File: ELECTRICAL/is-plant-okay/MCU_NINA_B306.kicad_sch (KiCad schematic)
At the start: 1 part

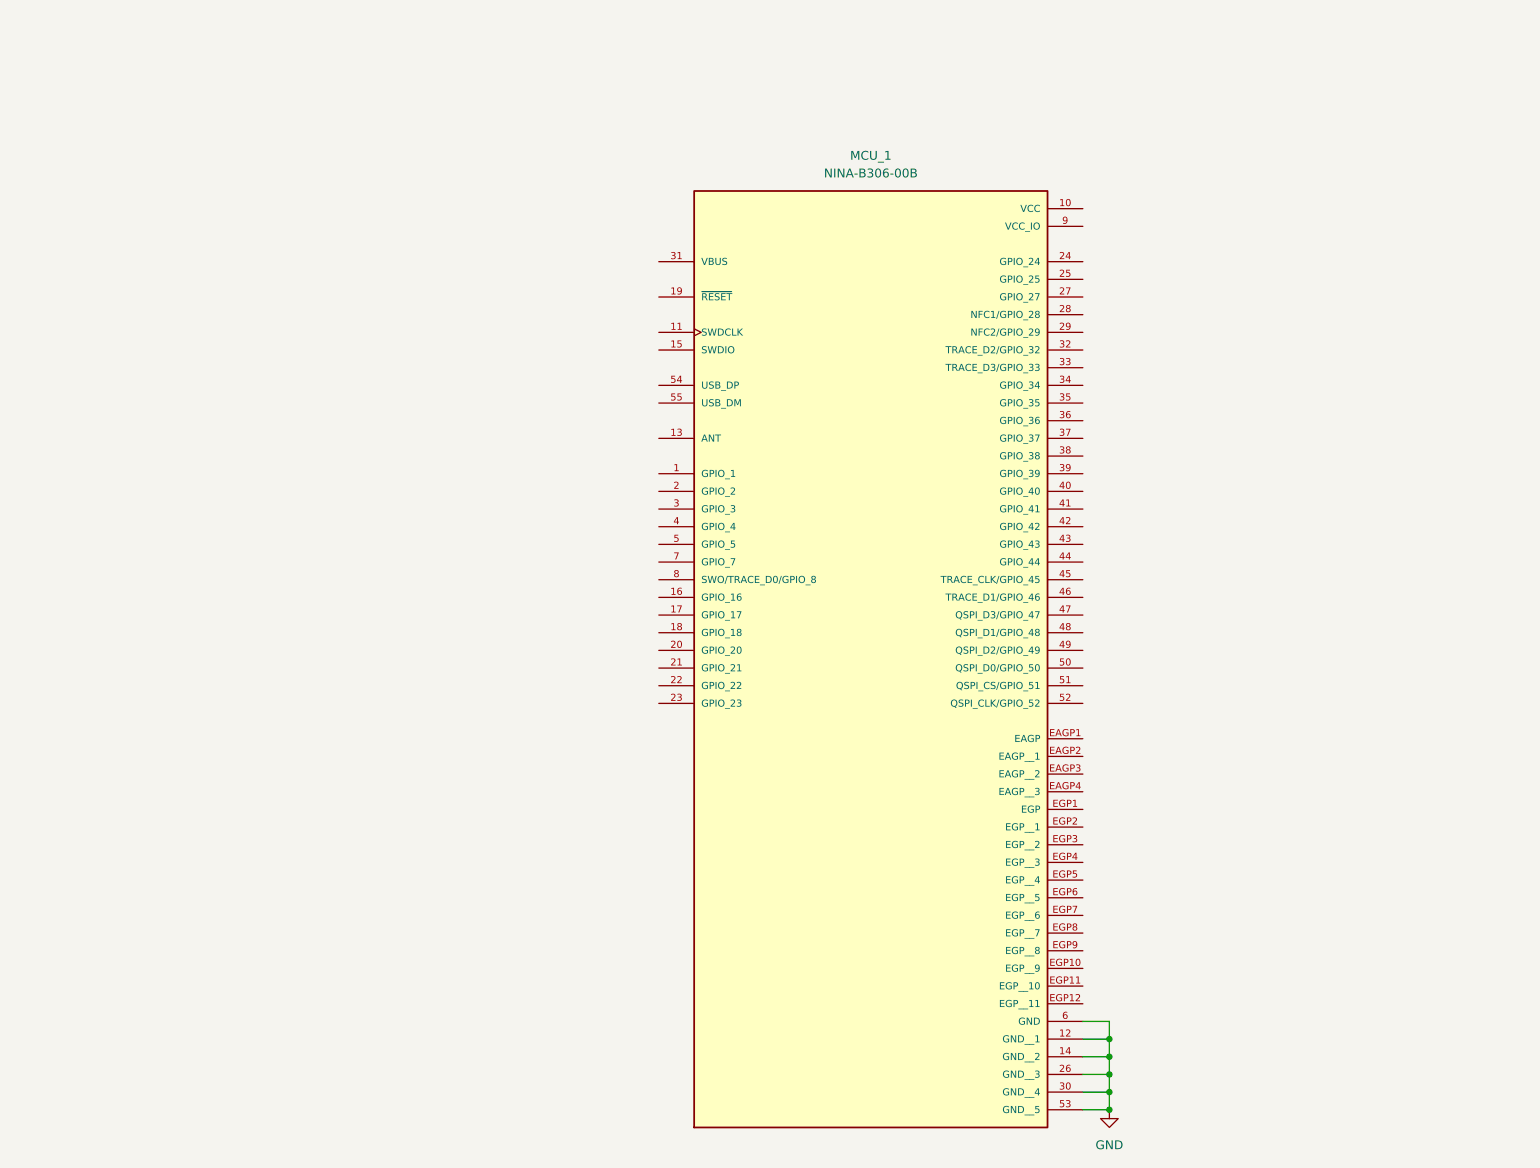
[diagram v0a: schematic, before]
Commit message: feat: add pins for mcu
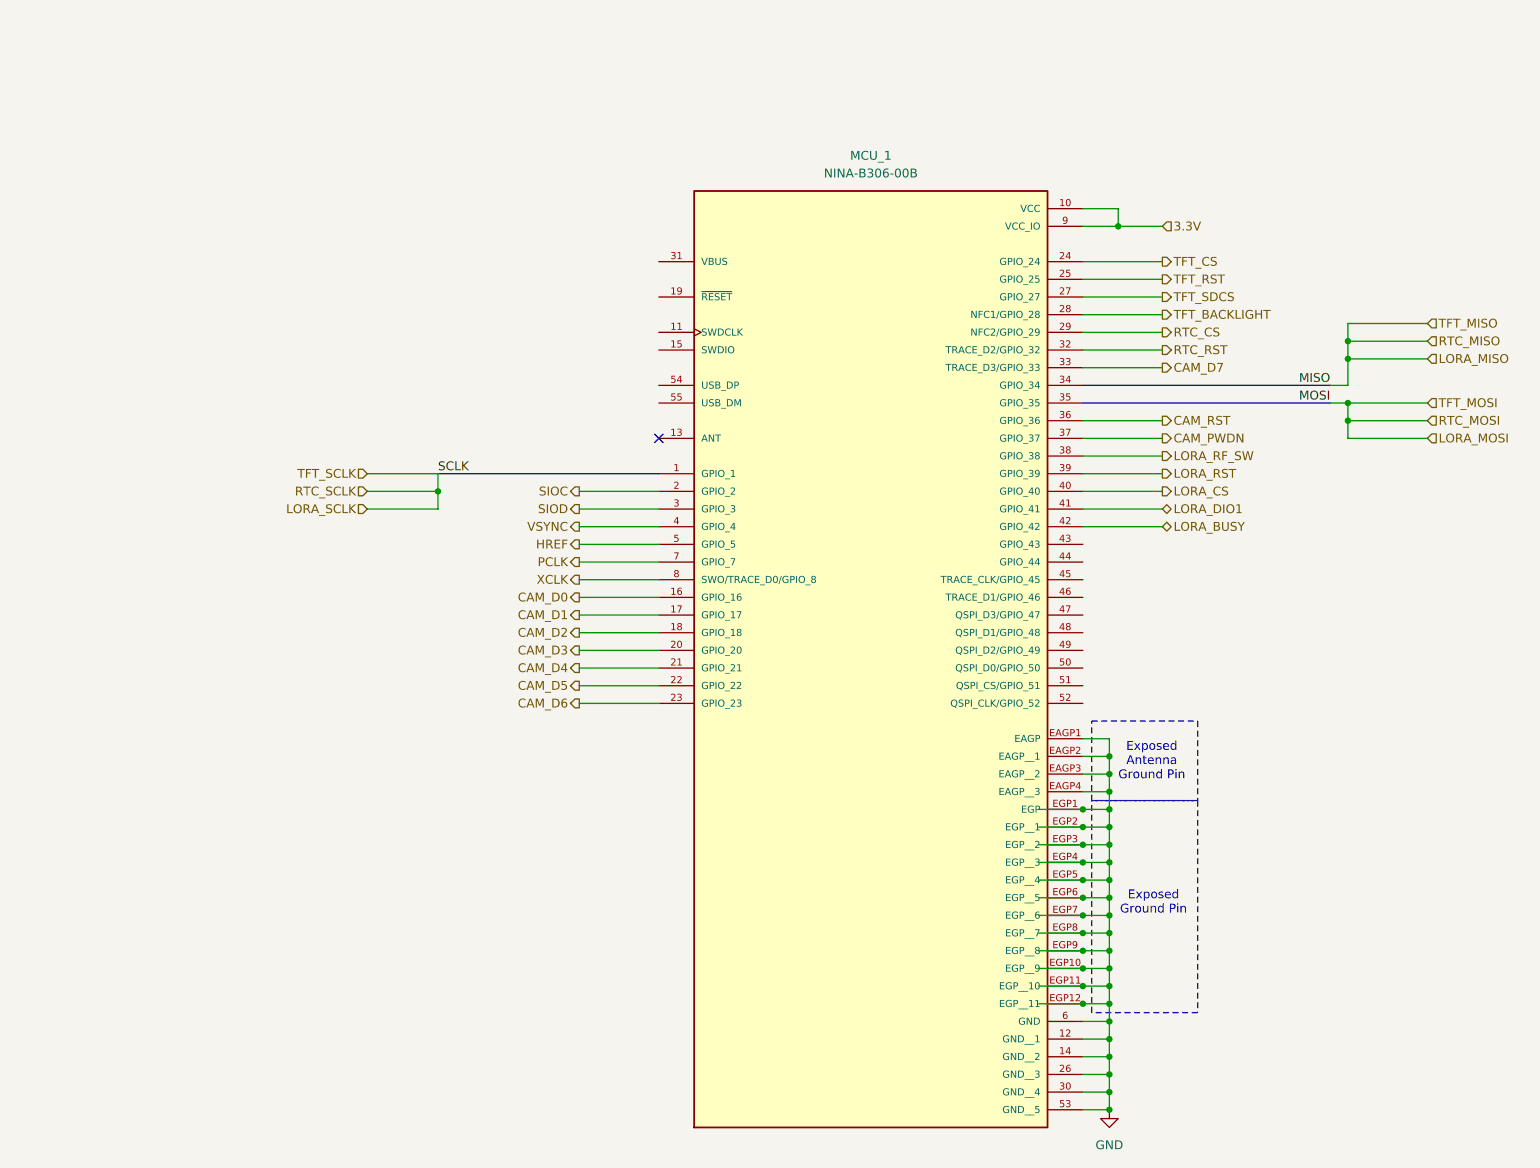
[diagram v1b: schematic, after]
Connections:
- net GND: now also MCU_1.EAGP1 (EAGP), MCU_1.EAGP2 (EAGP__1), MCU_1.EAGP3 (EAGP__2), MCU_1.EAGP4 (EAGP__3), MCU_1.EGP1 (EGP), MCU_1.EGP10 (EGP__9), MCU_1.EGP11 (EGP__10), MCU_1.EGP12 (EGP__11), MCU_1.EGP2 (EGP__1), MCU_1.EGP3 (EGP__2), MCU_1.EGP4 (EGP__3), MCU_1.EGP5 (EGP__4), MCU_1.EGP6 (EGP__5), MCU_1.EGP7 (EGP__6), MCU_1.EGP8 (EGP__7), MCU_1.EGP9 (EGP__8)
- net 3.3V: now reaches MCU_1.10 (VCC)
- net 3.3V: now also MCU_1.9 (VCC_IO)
- net CAM_D0: now reaches MCU_1.16 (GPIO_16)
- net CAM_D1: now reaches MCU_1.17 (GPIO_17)
- net CAM_D2: now reaches MCU_1.18 (GPIO_18)
- net SIOC: now reaches MCU_1.2 (GPIO_2)
- net CAM_D3: now reaches MCU_1.20 (GPIO_20)
- net CAM_D4: now reaches MCU_1.21 (GPIO_21)
- net CAM_D5: now reaches MCU_1.22 (GPIO_22)
- net CAM_D6: now reaches MCU_1.23 (GPIO_23)
- net TFT_CS: now reaches MCU_1.24 (GPIO_24)
- net TFT_RST: now reaches MCU_1.25 (GPIO_25)
- net TFT_SDCS: now reaches MCU_1.27 (GPIO_27)
- net TFT_BACKLIGHT: now reaches MCU_1.28 (NFC1/GPIO_28)
- net RTC_CS: now reaches MCU_1.29 (NFC2/GPIO_29)
- net SIOD: now reaches MCU_1.3 (GPIO_3)
- net RTC_RST: now reaches MCU_1.32 (TRACE_D2/GPIO_32)
- net CAM_D7: now reaches MCU_1.33 (TRACE_D3/GPIO_33)
- net CAM_RST: now reaches MCU_1.36 (GPIO_36)
- net CAM_PWDN: now reaches MCU_1.37 (GPIO_37)
- net LORA_RF_SW: now reaches MCU_1.38 (GPIO_38)
- net LORA_RST: now reaches MCU_1.39 (GPIO_39)
- net VSYNC: now reaches MCU_1.4 (GPIO_4)
- net LORA_CS: now reaches MCU_1.40 (GPIO_40)
- net LORA_DIO1: now reaches MCU_1.41 (GPIO_41)
- net LORA_BUSY: now reaches MCU_1.42 (GPIO_42)
- net HREF: now reaches MCU_1.5 (GPIO_5)
- net PCLK: now reaches MCU_1.7 (GPIO_7)
- net XCLK: now reaches MCU_1.8 (SWO/TRACE_D0/GPIO_8)
- no-connect marks 0 -> 1
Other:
- note added: "Exposed Antenna Ground Pin"
- note added: "Exposed Ground Pin"

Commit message: feat: add pins for bootloader programmer
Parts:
- added D1: TEST_LED, symbol Device:LED
- added J1: TSW-104-07-F-D, is-plant-okay-foot:SAMTEC_TSW-104-07-F-D, symbol is-plant-okay-lib:TSW-104-07-F-D
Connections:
- net GND: now also D1.1 (K); no longer MCU_1.53 (GND__5)
- net SWD_CLK: now reaches MCU_1.11 (SWDCLK)
- net SWD_CLK: now also J1.04
- net SWD_IO: now reaches MCU_1.15 (SWDIO)
- net SWD_IO: now also J1.02
- net N_RST: now reaches MCU_1.19 (~{RESET})
- net 5V: now reaches MCU_1.31 (VBUS)
- net at MCU_1.52 (QSPI_CLK/GPIO_52): now also D1.2 (A)
- net DATA_POS: now reaches MCU_1.54 (USB_DP)
- net DATA_NEG: now reaches MCU_1.55 (USB_DM)
- new net SWD_GND: J1.03, J1.05, MCU_1.53 (GND__5)
- no-connect marks 1 -> 10

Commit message: feat: finished schematics
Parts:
- added SW3: MCU_RST, symbol Switch:SW_Push
- added TP1: MCU_5V_TP, TestPoint:TestPoint_Keystone_5000-5004_Miniature, symbol Connector:TestPoint
- added TP2: MCU_3.3V_TP, TestPoint:TestPoint_Keystone_5000-5004_Miniature, symbol Connector:TestPoint
- added TP4: GND_TP, TestPoint:TestPoint_Keystone_5000-5004_Miniature, symbol Connector:TestPoint
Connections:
- net SWD_GND is gone; now on net GND: J1.03, J1.05, MCU_1.53 (GND__5)
- net 3.3V: now also J1.01, TP2.1
- net 5V: now also TP1.1
- net GND: now also SW3.1, TP4.1
- net LORA_MISO: now also MCU_1.34 (GPIO_34)
- net LORA_MOSI: now also MCU_1.35 (GPIO_35)
- net LORA_SCLK: now also MCU_1.1 (GPIO_1)
- net N_RST: now also J1.06, SW3.2
- net LORA_RST: no longer names the net of MCU_1.39 (GPIO_39)
- net RTC_RST: no longer names the net of MCU_1.32 (TRACE_D2/GPIO_32)
- net TFT_RST renamed TFT_DC
- no-connect marks 10 -> 14
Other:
- note added: "CMSIS-DAP Port"
- moved on the sheet: J1

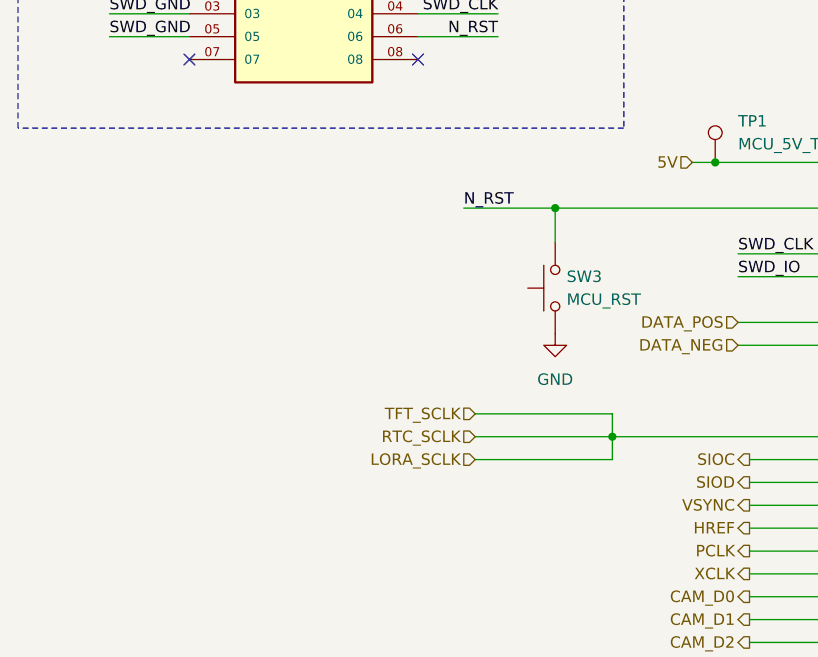
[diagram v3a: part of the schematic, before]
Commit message: feat: add resistor footprint
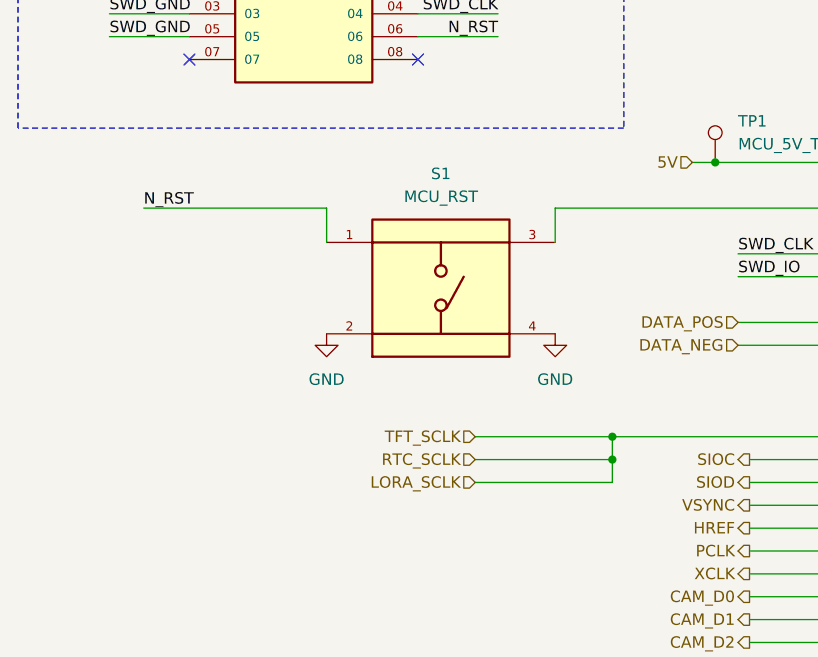
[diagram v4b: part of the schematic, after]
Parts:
- removed SW3: MCU_RST, symbol Switch:SW_Push
- added S1: MCU_RST, is-plant-okay-foot:SW_TS04-66-55-BK-260-SMT, symbol is-plant-okay-lib:TS04-66-55-BK-260-SMT
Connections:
- net GND: now also S1.2, S1.4
- net N_RST: now also S1.1; no longer MCU_1.19 (~{RESET})
- new net: MCU_1.19 (~{RESET}), S1.3

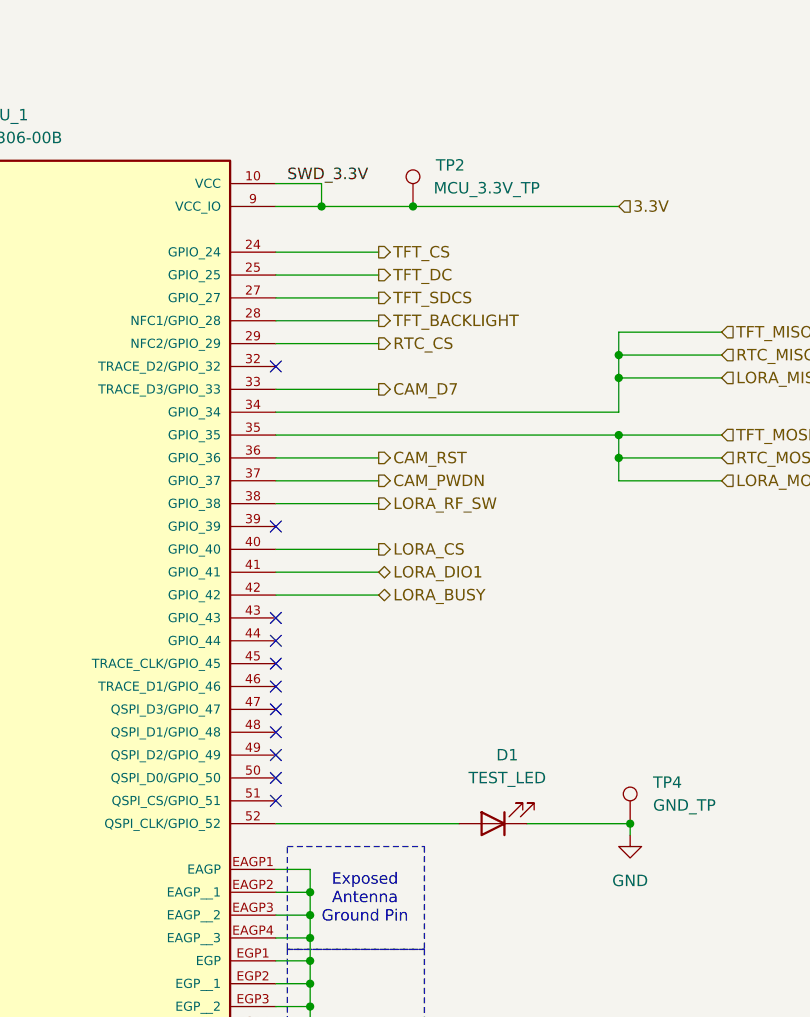
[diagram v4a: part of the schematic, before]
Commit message: feat: add remaining resistor, capacitor footprints
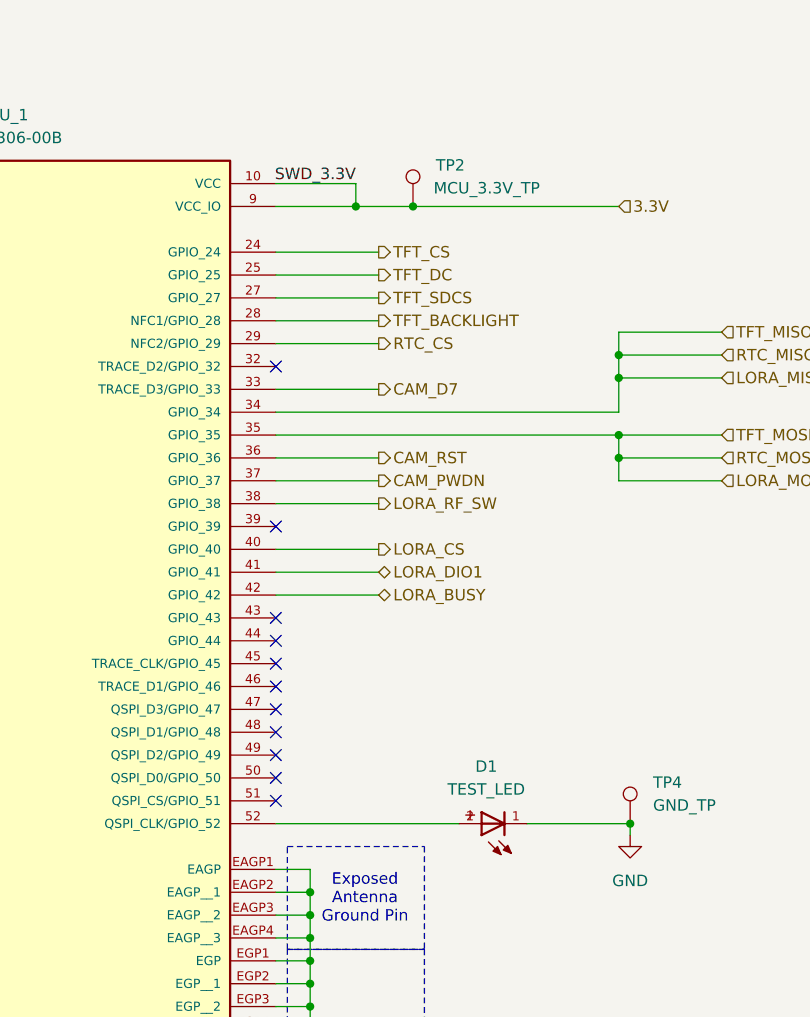
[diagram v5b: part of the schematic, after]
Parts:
- removed D1: TEST_LED, symbol Device:LED
- added D1: TEST_LED, is-plant-okay-foot:150120GS75000, symbol is-plant-okay-lib:WL-SMCW_1206
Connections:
- net GND: now also D1.1
- net at MCU_1.52 (QSPI_CLK/GPIO_52): now also D1.2
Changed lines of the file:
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@@
+	)
+	(junction
+		(at 176.53 43.18)
+		(diameter 0)
+		(color 0 0 0 0)
 	)
 	(junction
@@
 	(junction
 		(at 205.74 62.23)
-		(diameter 0)
-		(color 0 0 0 0)
-	)
-	(junction
-		(at 172.72 43.18)
 		(diameter 0)
 		(color 0 0 0 0)
@@
 	(wire
 		(pts
-			(xy 172.72 43.18) (xy 182.88 43.18)
+			(xy 167.64 40.64) (xy 176.53 40.64)
 		)
 		(stroke
@@
 	(wire
 		(pts
-			(xy 172.72 40.64) (xy 172.72 43.18)
+			(xy 176.53 40.64) (xy 176.53 43.18)
 		)
 		(stroke
@@
 	(wire
 		(pts
-			(xy 167.64 40.64) (xy 172.72 40.64)
-		)
-		(stroke
-			(width 0)
-			(type default)
-		)
-	)
-	(wire
-		(pts
 			(xy 167.64 73.66) (xy 179.07 73.66)
 		)
@@
 	(wire
 		(pts
-			(xy 167.64 43.18) (xy 172.72 43.18)
+			(xy 167.64 43.18) (xy 176.53 43.18)
 		)
 		(stroke
@@
 		(pts
 			(xy 80.01 78.74) (xy 80.01 81.28)
+		)
+		(stroke
+			(width 0)
+			(type default)
+		)
+	)
+	(wire
+		(pts
+			(xy 176.53 43.18) (xy 182.88 43.18)
 		)
 		(stroke
@@
 	)
 	(label "SWD_3.3V"
-		(at 168.91 40.64 0)
-		(effects
-			(font
-				(size 1.27 1.27)
-			)
-			(justify left bottom)
+		(at 176.53 40.64 180)
+		(effects
+			(font
+				(size 1.27 1.27)
+			)
+			(justify right bottom)
 		)
 	)
@@
 	)
 	(symbol
-		(lib_id "Device:LED")
-		(at 191.77 111.76 180)
-		(unit 1)
-		(exclude_from_sim no)
-		(in_bom yes)
-		(on_board yes)
-		(dnp no)
-		(fields_autoplaced yes)
-		(property "Reference" "D1"
-			(at 193.3575 104.14 0)
-			(effects
-				(font
-					(size 1.27 1.27)
-				)
-			)
-		)
-		(property "Value" "TEST_LED"
-			(at 193.3575 106.68 0)
-			(effects
-				(font
-					(size 1.27 1.27)
-				)
-			)
-		)
-		(property "Footprint" ""
-			(at 191.77 111.76 0)
-			(effects
-				(font
-					(size 1.27 1.27)
-				)
-				(hide yes)
-			)
-		)
-		(property "Datasheet" "~"
-			(at 191.77 111.76 0)
-			(effects
-				(font
-					(size 1.27 1.27)
-				)
-				(hide yes)
-			)
-		)
-		(property "Description" "Light emitting diode"
-			(at 191.77 111.76 0)
-			(effects
-				(font
-					(size 1.27 1.27)
-				)
-				(hide yes)
-			)
-		)
-		(property "Sim.Pins" "1=K 2=A"
-			(at 191.77 111.76 0)
-			(effects
-				(font
-					(size 1.27 1.27)
-				)
-				(hide yes)
-			)
-		)
-		(pin "2"
-		)
-		(pin "1"
-		)
-		(instances
-			(project ""
-				(path "/ac51c2f9-77a4-4b89-b63f-6e0ba02b1e45/f0d7ceea-66a9-4232-906e-fc203451d9a2"
-					(reference "D1")
-					(unit 1)
-				)
-			)
-		)
-	)
-	(symbol
 		(lib_id "Connector:TestPoint")
 		(at 182.88 43.18 0)
@@
 					(unit 1)
 				)
+			)
+		)
+	)
+	(symbol
+		(lib_id "is-plant-okay-lib:WL-SMCW_1206")
+		(at 193.04 111.76 180)
+		(unit 1)
+		(exclude_from_sim no)
+		(in_bom yes)
+		(on_board yes)
+		(dnp no)
+		(fields_autoplaced yes)
+		(property "Reference" "D1"
+			(at 191.0217 105.41 0)
+			(effects
+				(font
+					(size 1.27 1.27)
+				)
+			)
+		)
+		(property "Value" "TEST_LED"
+			(at 191.0217 107.95 0)
+			(effects
+				(font
+					(size 1.27 1.27)
+				)
+			)
+		)
+		(property "Footprint" "is-plant-okay-foot:150120GS75000"
+			(at 193.04 111.76 0)
+			(effects
+				(font
+					(size 1.27 1.27)
+				)
+				(justify bottom)
+				(hide yes)
+			)
+		)
+		(property "Datasheet" "https://www.we-online.com/components/products/datasheet/150120GS75000.pdf"
+			(at 193.04 111.76 0)
+			(effects
+				(font
+					(size 1.27 1.27)
+				)
+				(hide yes)
+			)
+		)
+		(property "Description" "LED GREEN CLEAR 1206 SMD"
+			(at 193.04 111.76 0)
+			(effects
+				(font
+					(size 1.27 1.27)
+				)
+				(hide yes)
+			)
+		)
+		(property "MFG PART #" "150120GS75000"
+			(at 193.04 111.76 0)
+			(effects
+				(font
+					(size 1.27 1.27)
+				)
+				(hide yes)
+			)
+		)
+		(property "MANUFACTURER" "Würth Elektronik"
+			(at 193.04 111.76 0)
+			(effects
+				(font
+					(size 1.27 1.27)
+				)
+				(hide yes)
+			)
+		)
+		(property "TYPE" "SMD"
+			(at 193.04 111.76 0)
+			(effects
+				(font
+					(size 1.27 1.27)
+				)
+				(hide yes)
+			)
+		)
+		(property "PACKAGE" "1206"
+			(at 193.04 111.76 0)
+			(effects
+				(font
+					(size 1.27 1.27)
+				)
+				(hide yes)
+			)
+		)
+		(pin "1"
+		)
+		(pin "2"
+		)
+		(instances
+			(project ""
+				(path "/ac51c2f9-77a4-4b89-b63f-6e0ba02b1e45/f0d7ceea-66a9-4232-906e-fc203451d9a2"
+					(reference "D1")
+					(unit 1)
+				)
